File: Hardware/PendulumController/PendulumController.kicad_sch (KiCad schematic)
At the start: 19 parts, among them J101 MOTOR, J102 ENCODER, Q101 MMBT3904, Q102 MMBT3906

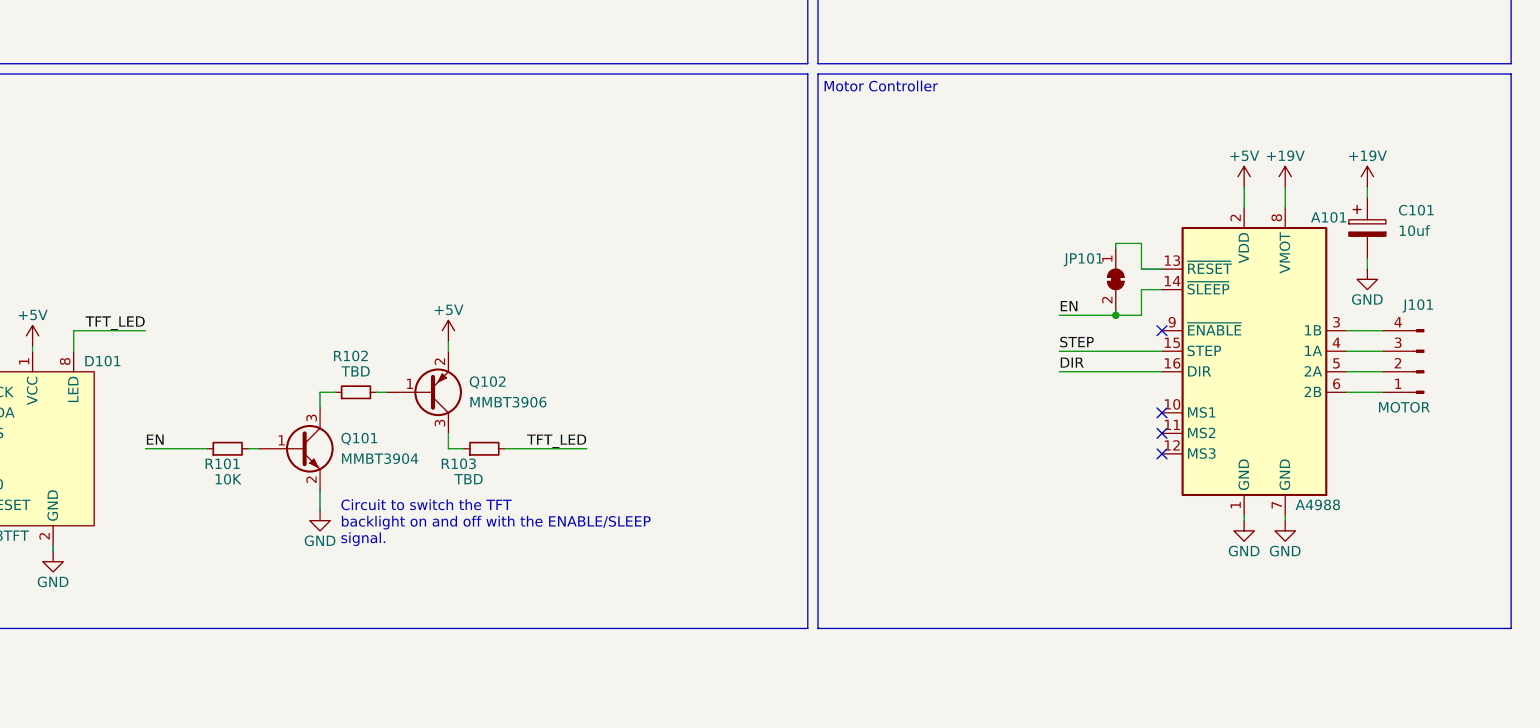
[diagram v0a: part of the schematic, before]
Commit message: Configure all pins
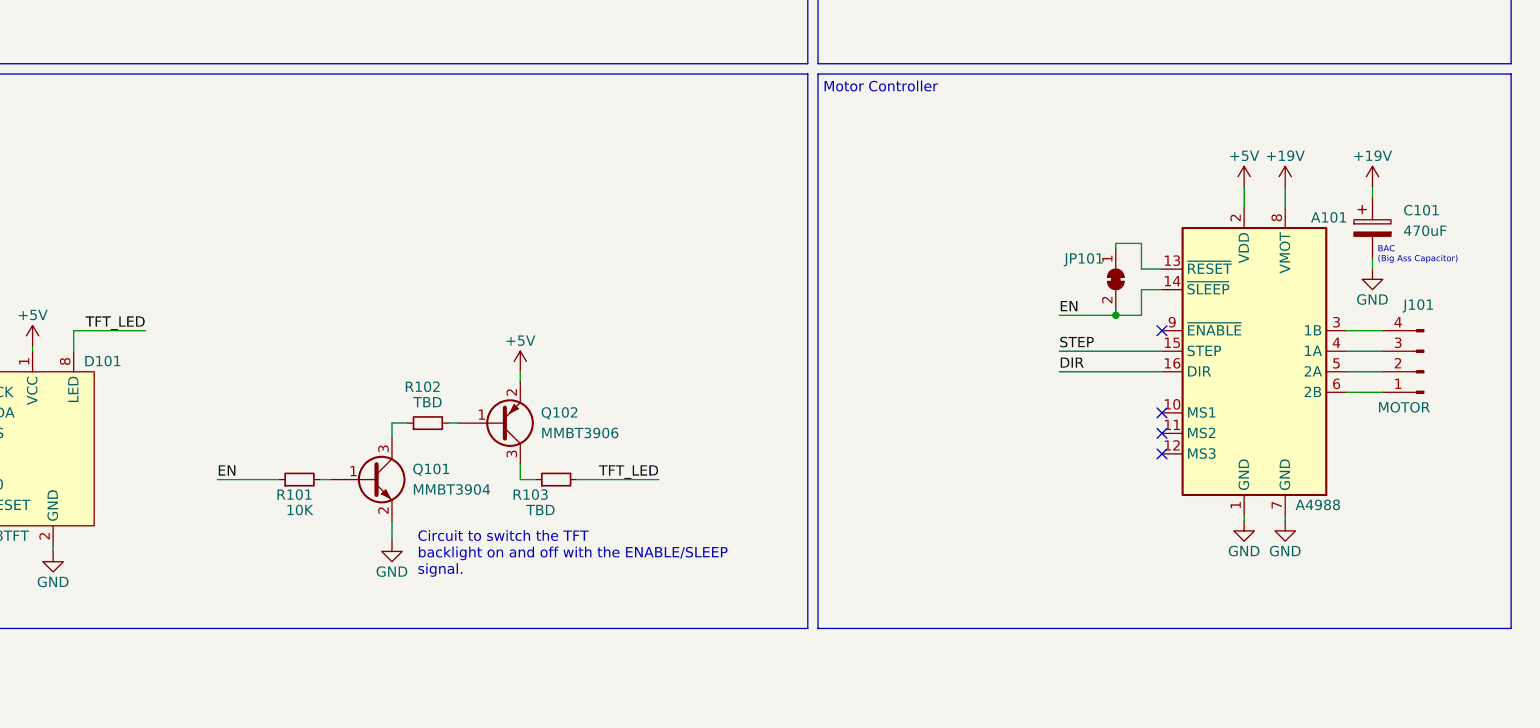
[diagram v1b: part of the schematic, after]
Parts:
- C101: value 10uf -> 470uF
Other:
- note added: "BAC (Big Ass Capacitor)"
- moved on the sheet: C101, Q101, Q102, R101, R102, R103
